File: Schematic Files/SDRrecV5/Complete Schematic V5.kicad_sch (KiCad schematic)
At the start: 73 parts, among them J1 Conn_Coaxial, J2 SJ1-3525N, U1 Si5351A-B-GT, U2 SN74CBT3253, U3 LT6231, U4 LM4562MA, Y1 Crystal_GND24_Small

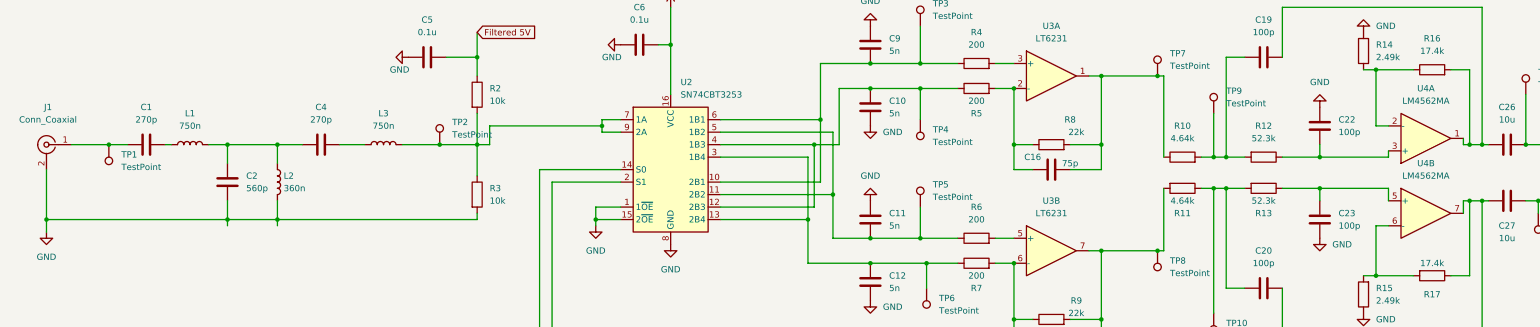
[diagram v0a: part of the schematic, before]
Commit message: Renamed Versions of our schematics
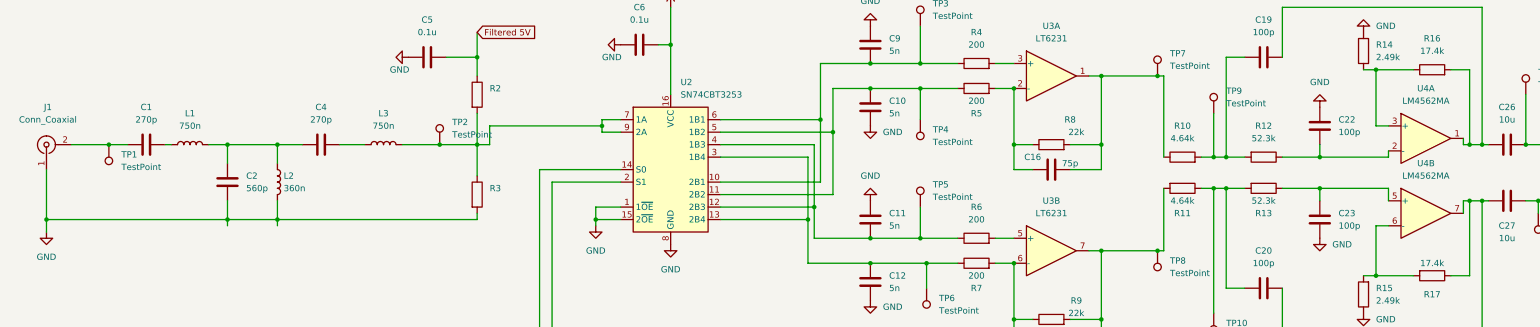
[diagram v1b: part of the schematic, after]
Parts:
- R2, R3: value 10k -> (none); footprint Resistor_SMD:R_2512_6332Metric -> (none)
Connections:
- net GND: now also J1.1 (In); no longer J1.2 (Ext)
- net at C1.2, TP1.1: now also J1.2 (Ext); no longer J1.1 (In)
- net at C10.2, R5.1, TP4.1: now also U2.11 (2B2), U2.5 (1B2); no longer U2.12 (2B3), U2.4 (1B3)
- net at R14.1, R16.1: now also U4.3 (+); no longer U4.2 (-)
- net at C11.1, R6.1, TP5.1: now also U2.12 (2B3), U2.4 (1B3); no longer U2.11 (2B2), U2.5 (1B2)
- net at C22.1, R12.1: now also U4.2 (-); no longer U4.3 (+)
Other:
- moved on the sheet: J1
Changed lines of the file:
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@@
   (junction (at 336.55 180.34) (diameter 0) (color 0 0 0 0)
   )
+  (junction (at 213.36 68.58) (diameter 0) (color 0 0 0 0)
+  )
   (junction (at 266.7 24.13) (diameter 0) (color 0 0 0 0)
   )
@@
   (junction (at 365.76 43.18) (diameter 0) (color 0 0 0 0)
   )
-  (junction (at 205.74 90.17) (diameter 0) (color 0 0 0 0)
-  )
   (junction (at 271.78 101.6) (diameter 0) (color 0 0 0 0)
   )
@@
   (junction (at 209.55 189.23) (diameter 0) (color 0 0 0 0)
   )
+  (junction (at 201.93 92.71) (diameter 0) (color 0 0 0 0)
+  )
   (junction (at 242.57 68.58) (diameter 0) (color 0 0 0 0)
   )
@@
   (junction (at 231.14 179.07) (diameter 0) (color 0 0 0 0)
   )
-  (junction (at 213.36 68.58) (diameter 0) (color 0 0 0 0)
-  )
   (junction (at 335.28 80.01) (diameter 0) (color 0 0 0 0)
   )
@@
   (junction (at 209.55 181.61) (diameter 0) (color 0 0 0 0)
   )
+  (junction (at 205.74 77.47) (diameter 0) (color 0 0 0 0)
+  )
   (junction (at 213.36 104.14) (diameter 0) (color 0 0 0 0)
   )
@@
   )
   (junction (at 213.36 63.5) (diameter 0) (color 0 0 0 0)
-  )
-  (junction (at 201.93 80.01) (diameter 0) (color 0 0 0 0)
   )
   (junction (at 69.85 158.75) (diameter 0) (color 0 0 0 0)
@@
   (no_connect (at 287.02 156.21))
   (no_connect (at 287.02 173.99))
+  (wire (pts (xy 205.74 68.58) (xy 205.74 77.47))
+    (stroke (width 0) (type default) (color 0 0 0 0))
+  )
   (wire (pts (xy 308.61 138.43) (xy 308.61 137.16))
     (stroke (width 0) (type default) (color 0 0 0 0))
@@
     (stroke (width 0) (type default) (color 0 0 0 0))
   )
-  (wire (pts (xy 205.74 99.06) (xy 213.36 99.06))
-    (stroke (width 0) (type default) (color 0 0 0 0))
-  )
   (wire (pts (xy 133.35 62.23) (xy 133.35 66.04))
     (stroke (width 0) (type default) (color 0 0 0 0))
@@
     (stroke (width 0) (type default) (color 0 0 0 0))
   )
-  (wire (pts (xy 207.01 80.01) (xy 207.01 68.58))
-    (stroke (width 0) (type default) (color 0 0 0 0))
-  )
   (wire (pts (xy 133.35 95.25) (xy 133.35 93.98))
     (stroke (width 0) (type default) (color 0 0 0 0))
@@
     (stroke (width 0) (type default) (color 0 0 0 0))
   )
+  (wire (pts (xy 201.93 92.71) (xy 201.93 99.06))
+    (stroke (width 0) (type default) (color 0 0 0 0))
+  )
   (wire (pts (xy 105.41 80.01) (xy 110.49 80.01))
     (stroke (width 0) (type default) (color 0 0 0 0))
@@
     (stroke (width 0) (type default) (color 0 0 0 0))
   )
-  (wire (pts (xy 205.74 90.17) (xy 205.74 99.06))
+  (wire (pts (xy 201.93 99.06) (xy 213.36 99.06))
     (stroke (width 0) (type default) (color 0 0 0 0))
   )
@@
     (stroke (width 0) (type default) (color 0 0 0 0))
   )
+  (wire (pts (xy 205.74 68.58) (xy 213.36 68.58))
+    (stroke (width 0) (type default) (color 0 0 0 0))
+  )
   (wire (pts (xy 224.79 109.22) (xy 224.79 104.14))
     (stroke (width 0) (type default) (color 0 0 0 0))
@@
     (stroke (width 0) (type default) (color 0 0 0 0))
   )
-  (wire (pts (xy 207.01 68.58) (xy 213.36 68.58))
-    (stroke (width 0) (type default) (color 0 0 0 0))
-  )
   (wire (pts (xy 231.14 176.53) (xy 231.14 179.07))
     (stroke (width 0) (type default) (color 0 0 0 0))
@@
   )
   (wire (pts (xy 157.48 95.25) (xy 157.48 96.52))
-    (stroke (width 0) (type default) (color 0 0 0 0))
-  )
-  (wire (pts (xy 201.93 80.01) (xy 207.01 80.01))
     (stroke (width 0) (type default) (color 0 0 0 0))
   )
@@
       (effects (font (size 1.27 1.27)) hide)
     )
-    (property "Datasheet" "https://www.te.com/commerce/DocumentDelivery/DDEController?Action=srchrtrv&DocNm=1773204&DocType=DS&DocLang=English" (id 3) (at 250.19 115.57 0)
+    (property "Datasheet" "https://www.meritekusa.com/wp-content/uploads/2018/06/Standard-Chip-Resistor-CR-Series.pdf" (id 3) (at 250.19 115.57 0)
       (effects (font (size 1.27 1.27)) hide)
     )
@@
       (effects (font (size 1.27 1.27)) hide)
     )
-    (property "Datasheet" "https://search.murata.co.jp/Ceramy/image/img/A01X/G101/ENG/GRM2195C1H512JA01-01.pdf" (id 3) (at 213.36 72.39 0)
+    (property "Datasheet" "https://datasheets.kyocera-avx.com/X7RDielectric.pdf" (id 3) (at 213.36 72.39 0)
       (effects (font (size 1.27 1.27)) hide)
     )
@@
       (effects (font (size 1.27 1.27)) hide)
     )
-    (property "Datasheet" "https://search.murata.co.jp/Ceramy/image/img/A01X/G101/ENG/GRM2195C1H512JA01-01.pdf" (id 3) (at 213.36 95.25 0)
+    (property "Datasheet" "https://datasheets.kyocera-avx.com/X7RDielectric.pdf" (id 3) (at 213.36 95.25 0)
       (effects (font (size 1.27 1.27)) hide)
     )
@@
     (pin "1")
   )
-  (symbol (lib_id "lt6231:LT6231") (at 326.39 78.74 0) (mirror x) (unit 1)
+  (symbol (lib_id "lt6231:LT6231") (at 326.39 78.74 0) (unit 1)
     (in_bom yes) (on_board yes) (fields_autoplaced)
     (property "Reference" "U4" (id 0) (at 326.39 68.58 0))
@@
       (effects (font (size 1.27 1.27)) hide)
     )
-    (property "Datasheet" "https://search.murata.co.jp/Ceramy/image/img/A01X/G101/ENG/GRM2195C1H512JA01-01.pdf" (id 3) (at 213.36 59.69 0)
+    (property "Datasheet" "https://datasheets.kyocera-avx.com/X7RDielectric.pdf" (id 3) (at 213.36 59.69 0)
       (effects (font (size 1.27 1.27)) hide)
     )
@@
     (pin "2")
   )
-  (symbol (lib_id "Connector:Conn_Coaxial") (at 45.72 80.01 0) (mirror y) (unit 1)
-    (in_bom yes) (on_board yes) (fields_autoplaced)
-    (property "Reference" "J1" (id 0) (at 46.0374 72.39 0))
-    (property "Value" "Conn_Coaxial" (id 1) (at 46.0374 74.93 0))
+  (symbol (lib_id "Connector:Conn_Coaxial") (at 45.72 80.01 90) (unit 1)
+    (in_bom yes) (on_board yes) (fields_autoplaced)
+    (property "Reference" "J1" (id 0) (at 46.0132 72.39 90))
+    (property "Value" "Conn_Coaxial" (id 1) (at 46.0132 74.93 90))
     (property "Footprint" "Connector_Coaxial:BNC_Amphenol_B6252HB-NPP3G-50_Horizontal" (id 2) (at 45.72 80.01 0)
       (effects (font (size 1.27 1.27)) hide)
@@
       (effects (font (size 1.27 1.27)) hide)
     )
-    (property "Datasheet" "https://search.murata.co.jp/Ceramy/image/img/A01X/G101/ENG/GRM2195C1H512JA01-01.pdf" (id 3) (at 213.36 107.95 0)
+    (property "Datasheet" "https://datasheets.kyocera-avx.com/X7RDielectric.pdf" (id 3) (at 213.36 107.95 0)
       (effects (font (size 1.27 1.27)) hide)
     )
@@
       (effects (font (size 1.27 1.27)) hide)
     )
-    (property "Datasheet" "https://www.te.com/commerce/DocumentDelivery/DDEController?Action=srchrtrv&DocNm=1773204&DocType=DS&DocLang=English" (id 3) (at 250.19 80.01 0)
+    (property "Datasheet" "https://www.meritekusa.com/wp-content/uploads/2018/06/Standard-Chip-Resistor-CR-Series.pdf" (id 3) (at 250.19 80.01 0)
       (effects (font (size 1.27 1.27)) hide)
     )
@@
       (effects (font (size 1.27 1.27)) (justify left))
     )
-    (property "Value" "10k" (id 1) (at 135.89 91.4399 0)
-      (effects (font (size 1.27 1.27)) (justify left))
-    )
-    (property "Footprint" "Resistor_SMD:R_2512_6332Metric" (id 2) (at 131.572 90.17 90)
+    (property "Value" "" (id 1) (at 135.89 91.4399 0)
+      (effects (font (size 1.27 1.27)) (justify left))
+    )
+    (property "Footprint" "" (id 2) (at 131.572 90.17 90)
       (effects (font (size 1.27 1.27)) hide)
     )
@@
       (effects (font (size 1.27 1.27)) (justify left))
     )
-    (property "Value" "10k" (id 1) (at 135.89 71.1199 0)
-      (effects (font (size 1.27 1.27)) (justify left))
-    )
-    (property "Footprint" "Resistor_SMD:R_2512_6332Metric" (id 2) (at 131.572 69.85 90)
-      (effects (font (size 1.27 1.27)) hide)
-    )
+    (property "Value" "" (id 1) (at 135.89 71.1199 0)
+      (effects (font (size 1.27 1.27)) (justify left))
+    )
+    (property "Footprint" "" (id 2) (at 131.572 69.85 90)
+      (effects (font (size 1.27 1.27)) hide)
+    )
